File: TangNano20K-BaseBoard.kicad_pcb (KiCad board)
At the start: 2 copper layers, 100 x 85 mm, 49 parts, among them J1 Conn_01x20_Socket, J2 Conn_01x20_Socket, J3 Conn_01x06_Socket, J4 Conn_01x06_Socket, Q1 PN2222A, Q2 PN2222A, Q3 PN2222A, Q4 PN2222A, SW1 SW_SPDT_321, SW2 SW_SPDT_321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

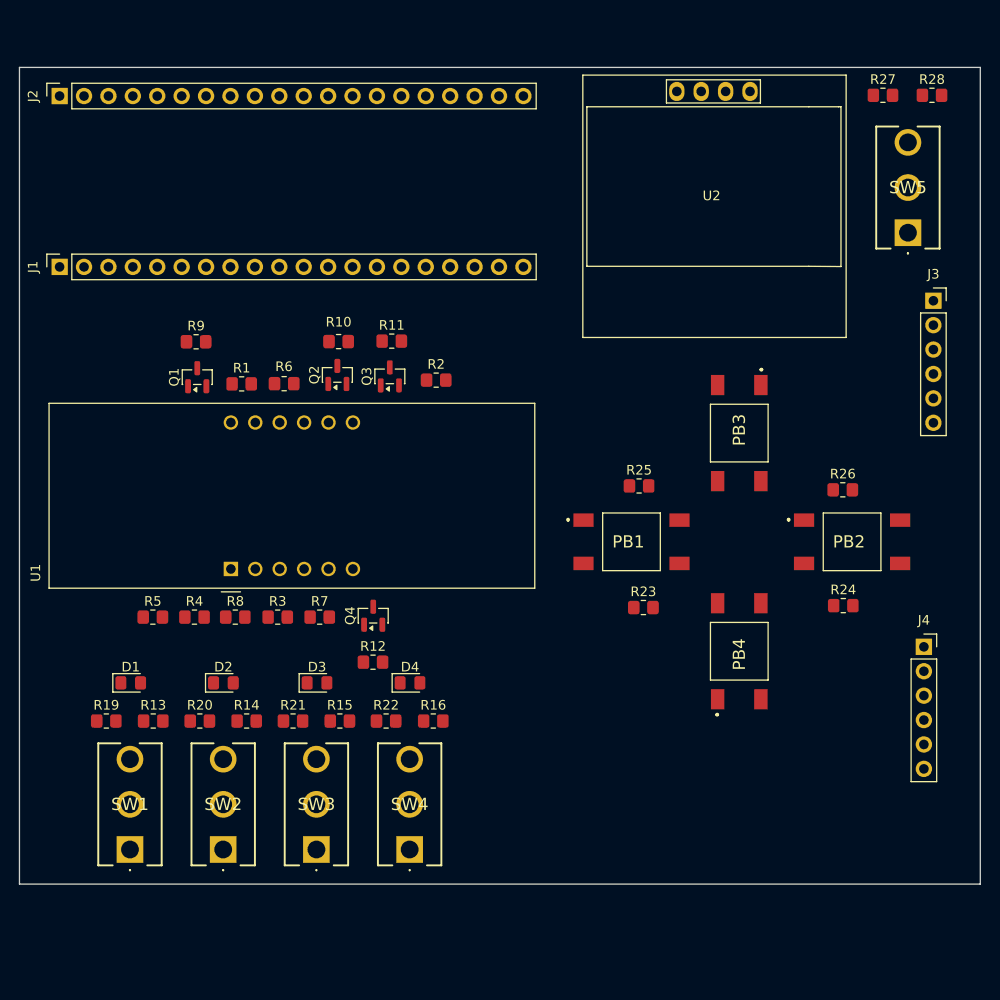
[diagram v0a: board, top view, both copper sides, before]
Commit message: Update SW1, SW2, SW3, SW4, SW5
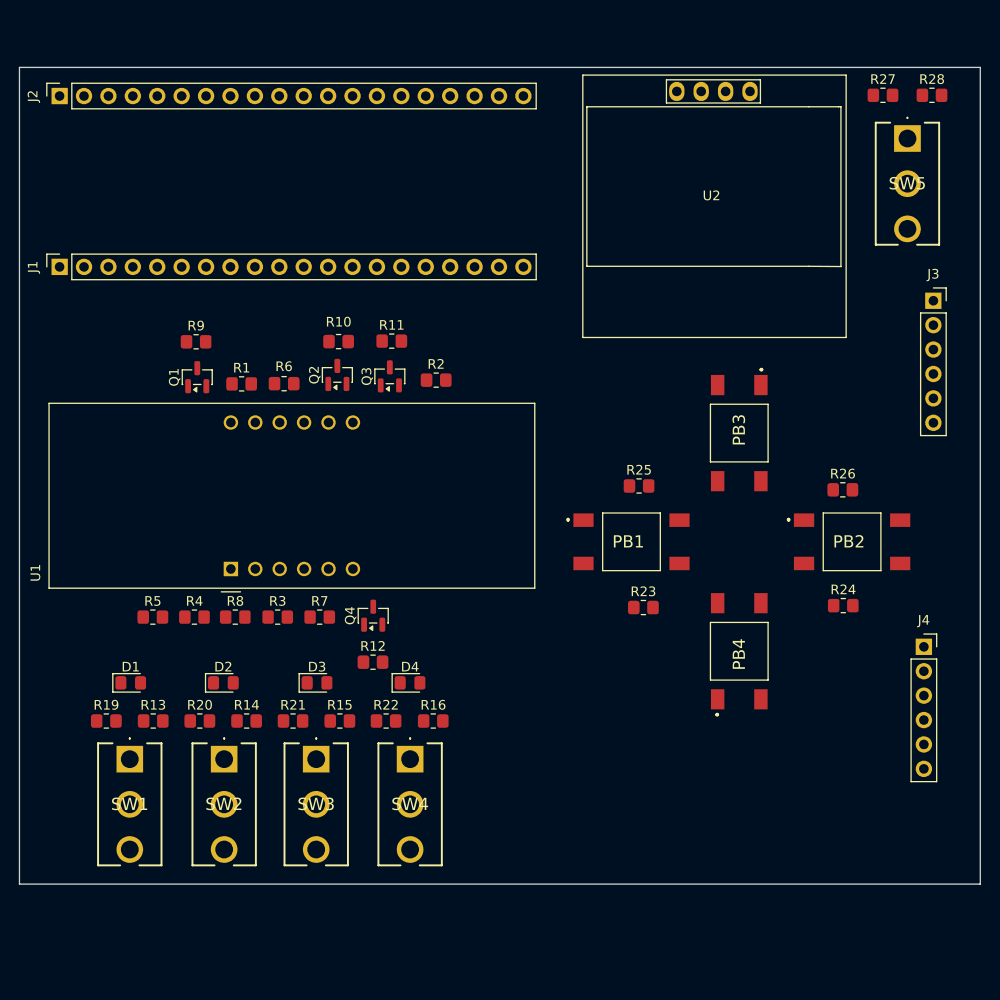
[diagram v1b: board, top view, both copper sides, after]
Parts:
- moved SW5 9.80 mm to (242.4, 82.4), turned to 180 degrees
- moved SW2 9.40 mm to (171.3, 147.0), turned to 180 degrees
- moved SW4 9.40 mm to (190.7, 147.0), turned to 180 degrees
- moved SW1 9.40 mm to (161.5, 147.0), turned to 180 degrees
- moved SW3 9.40 mm to (180.9, 147.0), turned to 180 degrees

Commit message: Update schematic and pcb
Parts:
- moved R26 21.2 mm to (218.2, 131.0)
- moved R25 17.4 mm to (231.9, 118.0)
- moved R23 13.6 mm to (218.2, 118.0)
- moved R27 5.04 mm to (244.9, 78.0)
- moved R28 5.03 mm to (239.9, 78.0)
- moved R24 3.85 mm to (231.9, 131.0)
- moved D1 3.27 mm to (164.8, 139.0)
- moved D2 3.27 mm to (174.5, 139.0)
- moved D4 3.27 mm to (193.9, 139.0)
- moved Q4 3.27 mm to (190.1, 132.1)
- moved R12 3.27 mm to (190.1, 136.9)
- moved R13 3.27 mm to (167.2, 143.0)
- moved R14 3.27 mm to (176.9, 143.0)
- moved R15 3.27 mm to (186.6, 143.0)
- moved R16 3.27 mm to (196.3, 143.0)
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
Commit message: Big Update
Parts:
- removed J4: Conn_01x06_Socket, Connector_PinSocket_2.54mm:PinSocket_1x06_P2.54mm_Vertical
- J3: value Conn_01x06_Socket -> Conn_02x06_Odd_Even; footprint Connector_PinSocket_2.54mm:PinSocket_1x06_P2.54mm_Vertical -> Connector_PinSocket_2.54mm:PinSocket_2x06_P2.54mm_Horizontal
- moved J3 62.4 mm to (236.9, 161.2), turned to 180 degrees
- moved PB3 50.3 mm to (209.1, 161.0), turned to 180 degrees
- moved R25 46.9 mm to (203.0, 155.0)
- moved J1 38.0 mm to (174.6, 127.8)
- moved J2 38.0 mm to (174.6, 110.0)
- moved R12 30.3 mm to (189.2, 106.6)
- moved Q1 30.3 mm to (167.0, 76.7)
- moved Q2 30.3 mm to (181.0, 76.7)
- moved Q3 30.3 mm to (187.0, 76.7)
- moved R1 30.3 mm to (172.4, 77.2)
- moved R10 30.3 mm to (181.2, 73.1)
- moved R11 30.3 mm to (187.0, 73.1)
- moved R6 30.3 mm to (176.8, 77.2)
- moved R9 30.3 mm to (167.0, 73.1)
- moved U1 30.3 mm to (171.9, 96.9)
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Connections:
- J3 pad 1: /80 -> +3V3
- J3 pad 2: /41 -> +3V3
- J3 pad 3: /55 -> GND
- J3 pad 4: /49 -> GND
- J3 pad 5: +3V3 -> /80
- J3 pad 6: GND -> /86
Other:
- board size 100 x 85 mm -> 100 x 100 mm
- board text added: "Q4"
